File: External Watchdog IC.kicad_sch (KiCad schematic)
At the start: 10 parts, among them U10 TPS3823A-33DBVR, U9 TPS3823A-33DBVR

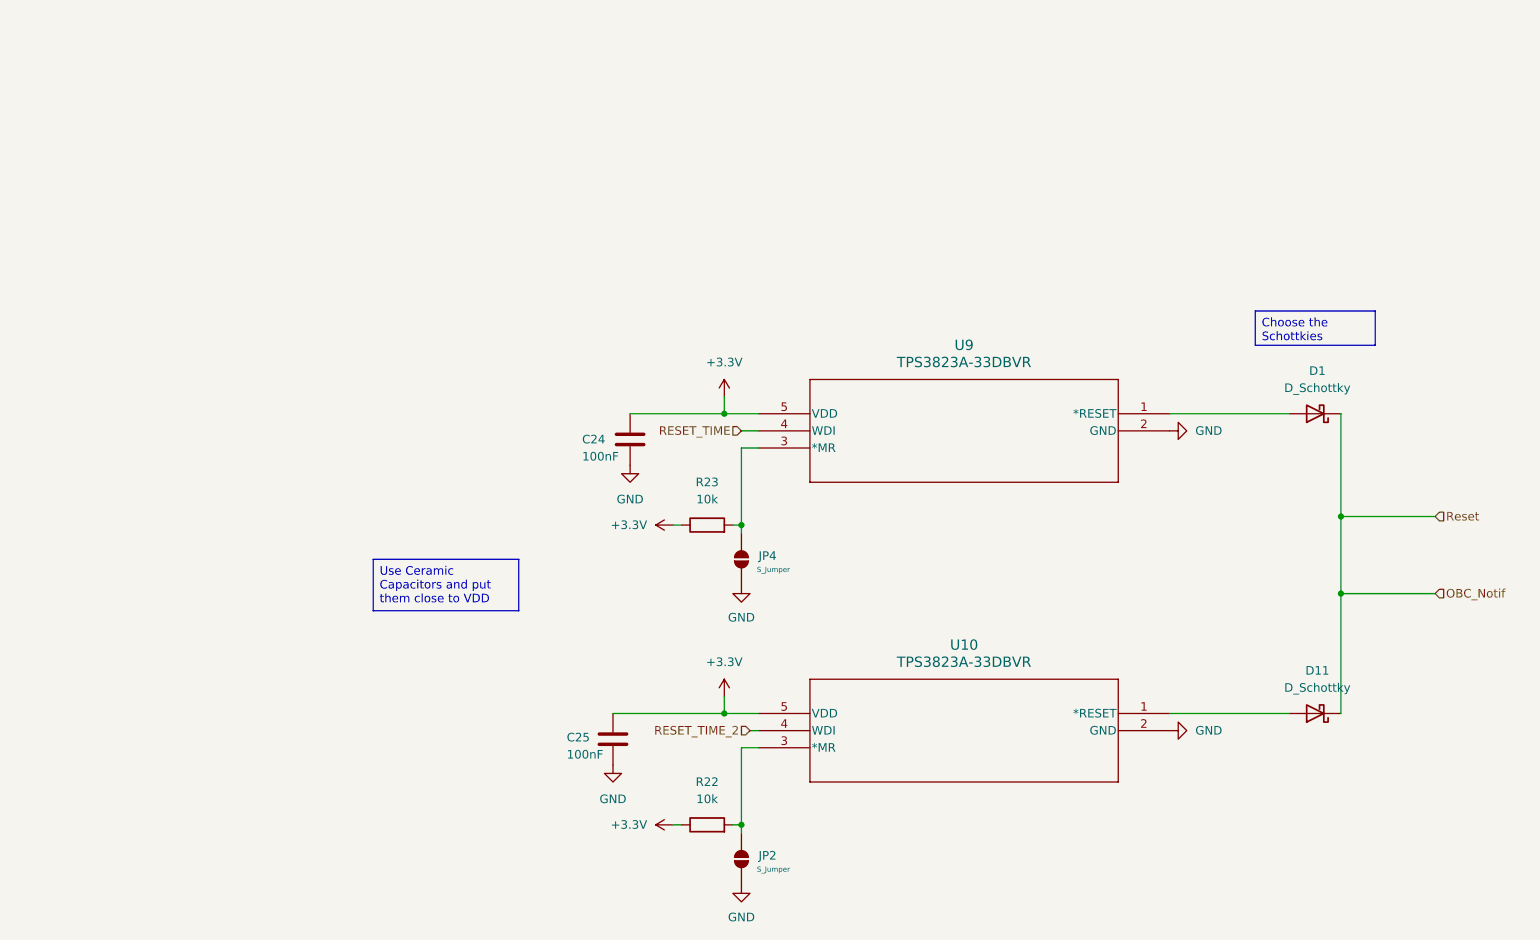
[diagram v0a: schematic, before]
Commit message: Added cap to output of lines
based on LTSpice Simulation
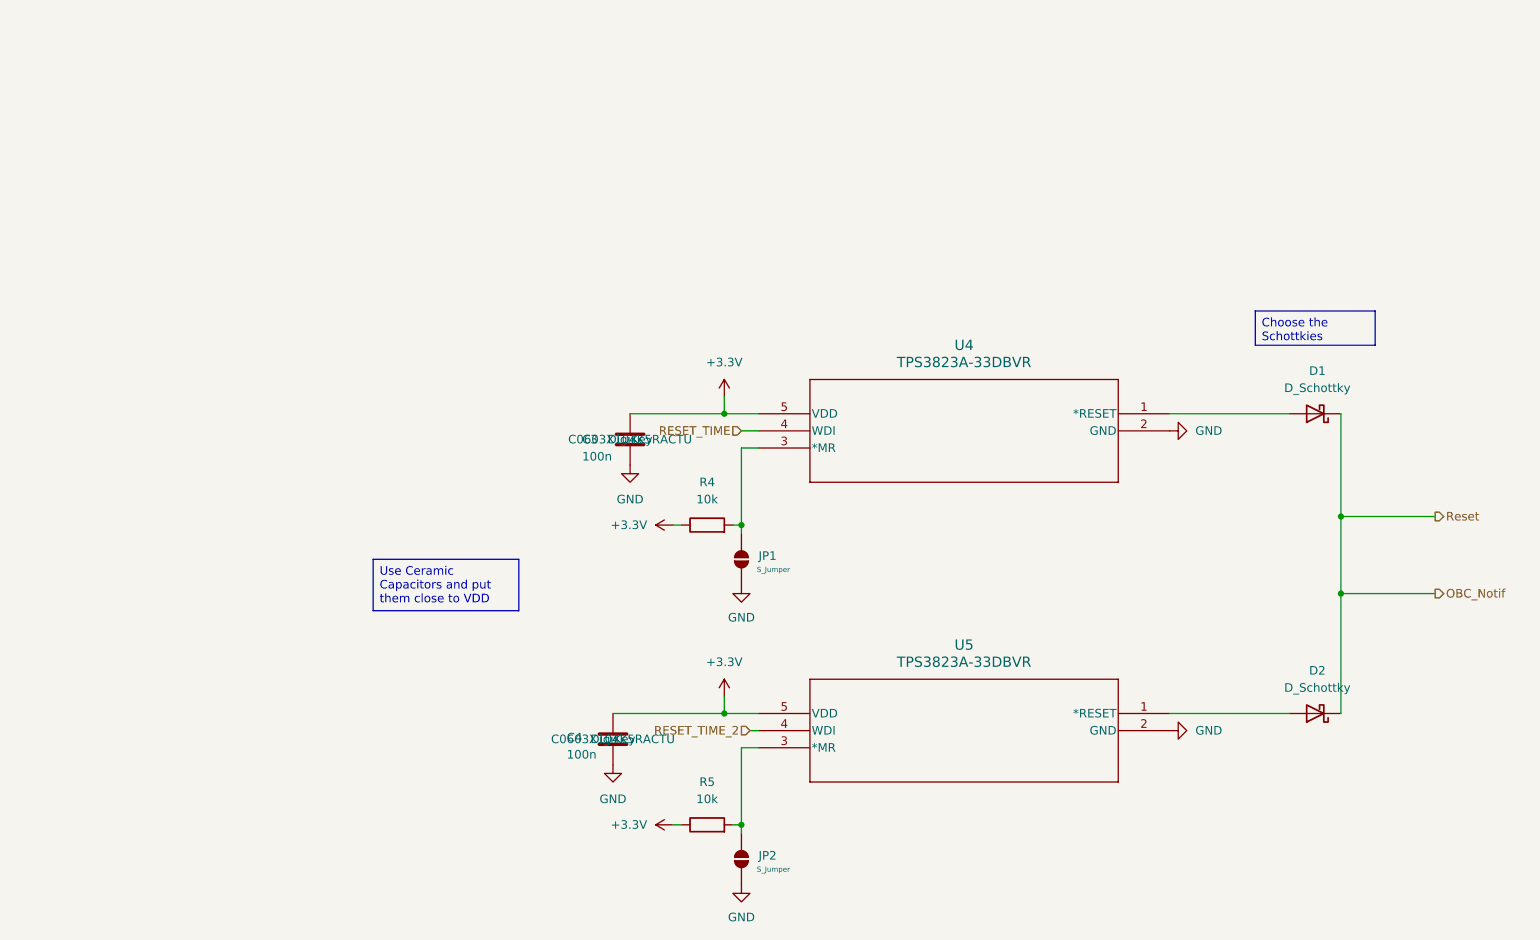
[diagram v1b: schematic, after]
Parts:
- C3: renamed from C24; value 100nF -> 100n; footprint (none) -> Capacitor_SMD:C_0603_1608Metric; MANUFACTURER (none) -> DigiKey; MANUFACTURER_PART_NUMBER (none) -> C0603X104K5RACTU
- C4: renamed from C25; value 100nF -> 100n; footprint (none) -> Capacitor_SMD:C_0603_1608Metric; MANUFACTURER (none) -> DigiKey; MANUFACTURER_PART_NUMBER (none) -> C0603X104K5RACTU
- U5: renamed from U10; footprint DBV5 -> DQC0010A
- renumbered D11 to D2, JP4 to JP1, R23 to R4, R22 to R5, U9 to U4
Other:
- company: (none) -> QSET (Jaron Cyna)
- title: (none) -> External Watchdog
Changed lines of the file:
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@@
 	(generator_version "9.0")
 	(paper "A4")
+	(title_block
+		(title "External Watchdog")
+		(date "2026-03-17")
+		(rev "1.0")
+		(company "QSET (Jaron Cyna)")
+	)
 	(text_box "Use Ceramic Capacitors and put them close to VDD"
 		(exclude_from_sim no)
@@
 	)
 	(hierarchical_label "Reset"
-		(shape input)
+		(shape output)
 		(at 220.98 87.63 0)
 		(effects
@@
 	)
 	(hierarchical_label "OBC_Notif"
-		(shape input)
+		(shape output)
 		(at 220.98 99.06 0)
 		(effects
@@
 		(dnp no)
 		(fields_autoplaced yes)
-		(property "Reference" "#PWR074"
+		(property "Reference" "#PWR016"
 			(at 111.76 133.35 0)
 			(effects
@@
 			(project "EPS_mppt_board"
 				(path "/8f246f89-1ec7-4136-9977-839b50e116ed/61eb8b07-a516-4600-8bd8-c85438ae98cc"
-					(reference "#PWR074")
+					(reference "#PWR016")
 					(unit 1)
 				)
@@
 		(dnp no)
 		(fields_autoplaced yes)
-		(property "Reference" "D11"
+		(property "Reference" "D2"
 			(at 203.5175 110.49 0)
 			(effects
@@
 			(project "EPS_mppt_board"
 				(path "/8f246f89-1ec7-4136-9977-839b50e116ed/61eb8b07-a516-4600-8bd8-c85438ae98cc"
-					(reference "D11")
+					(reference "D2")
 					(unit 1)
 				)
@@
 		(dnp no)
 		(fields_autoplaced yes)
-		(property "Reference" "#PWR071"
+		(property "Reference" "#PWR014"
 			(at 187.96 119.38 0)
 			(effects
@@
 			(project "EPS_mppt_board"
 				(path "/8f246f89-1ec7-4136-9977-839b50e116ed/61eb8b07-a516-4600-8bd8-c85438ae98cc"
-					(reference "#PWR071")
+					(reference "#PWR014")
 					(unit 1)
 				)
@@
 		(dnp no)
 		(fields_autoplaced yes)
-		(property "Reference" "#PWR067"
+		(property "Reference" "#PWR010"
 			(at 101.6 86.36 0)
 			(effects
@@
 			(project ""
 				(path "/8f246f89-1ec7-4136-9977-839b50e116ed/61eb8b07-a516-4600-8bd8-c85438ae98cc"
-					(reference "#PWR067")
+					(reference "#PWR010")
 					(unit 1)
 				)
@@
 		(on_board yes)
 		(dnp no)
-		(property "Reference" "U10"
+		(property "Reference" "U5"
 			(at 151.13 106.68 0)
 			(effects
@@
 			)
 		)
-		(property "Footprint" "DBV5"
+		(property "Footprint" "DQC0010A"
 			(at 181.61 116.84 0)
 			(effects
@@
 			(project "EPS_mppt_board"
 				(path "/8f246f89-1ec7-4136-9977-839b50e116ed/61eb8b07-a516-4600-8bd8-c85438ae98cc"
-					(reference "U10")
+					(reference "U5")
 					(unit 1)
 				)
@@
 		(dnp no)
 		(fields_autoplaced yes)
-		(property "Reference" "R23"
+		(property "Reference" "R4"
 			(at 113.03 82.55 90)
 			(effects
@@
 			(project "EPS_mppt_board"
 				(path "/8f246f89-1ec7-4136-9977-839b50e116ed/61eb8b07-a516-4600-8bd8-c85438ae98cc"
-					(reference "R23")
+					(reference "R4")
 					(unit 1)
 				)
@@
 		(on_board yes)
 		(dnp no)
-		(property "Reference" "C24"
+		(property "Reference" "C3"
 			(at 94.488 76.2 0)
 			(effects
@@
 			)
 		)
-		(property "Value" "100nF"
+		(property "Value" "100n"
 			(at 94.488 78.74 0)
 			(effects
@@
 			)
 		)
-		(property "Footprint" ""
+		(property "Footprint" "Capacitor_SMD:C_0603_1608Metric"
 			(at 102.5652 80.01 0)
 			(effects
@@
 			)
 		)
-		(property "Datasheet" "~"
+		(property "Datasheet" "kicad-embed://KEM_C1013_X7R_FT-CAP_SMD.pdf"
 			(at 101.6 76.2 0)
 			(effects
@@
 			)
 		)
-		(property "Description" "Unpolarized capacitor"
+		(property "Description" "kicad-embed://KEM_C1013_X7R_FT-CAP_SMD.pdf"
 			(at 101.6 76.2 0)
 			(effects
@@
 			)
 		)
+		(property "MANUFACTURER" "DigiKey"
+			(at 101.6 76.2 0)
+			(effects
+				(font
+					(size 1.27 1.27)
+				)
+			)
+		)
+		(property "MANUFACTURER_PART_NUMBER" "C0603X104K5RACTU"
+			(at 101.6 76.2 0)
+			(effects
+				(font
+					(size 1.27 1.27)
+				)
+			)
+		)
 		(pin "1"
 		)
@@
 			(project ""
 				(path "/8f246f89-1ec7-4136-9977-839b50e116ed/61eb8b07-a516-4600-8bd8-c85438ae98cc"
-					(reference "C24")
+					(reference "C3")
 					(unit 1)
 				)
@@
 		(dnp no)
 		(fields_autoplaced yes)
-		(property "Reference" "#PWR066"
+		(property "Reference" "#PWR08"
 			(at 115.57 73.66 0)
 			(effects
@@
 			(project ""
 				(path "/8f246f89-1ec7-4136-9977-839b50e116ed/61eb8b07-a516-4600-8bd8-c85438ae98cc"
-					(reference "#PWR066")
+					(reference "#PWR08")
 					(unit 1)
 				)
@@
 		(dnp no)
 		(fields_autoplaced yes)
-		(property "Reference" "R22"
+		(property "Reference" "R5"
 			(at 113.03 127 90)
 			(effects
@@
 			(project ""
 				(path "/8f246f89-1ec7-4136-9977-839b50e116ed/61eb8b07-a516-4600-8bd8-c85438ae98cc"
-					(reference "R22")
+					(reference "R5")
 					(unit 1)
 				)
@@
 		(on_board yes)
 		(dnp no)
-		(property "Reference" "C25"
+		(property "Reference" "C4"
 			(at 92.202 120.396 0)
 			(effects
@@
 			)
 		)
-		(property "Value" "100nF"
+		(property "Value" "100n"
 			(at 92.202 122.936 0)
 			(effects
@@
 			)
 		)
-		(property "Footprint" ""
+		(property "Footprint" "Capacitor_SMD:C_0603_1608Metric"
 			(at 100.0252 124.46 0)
 			(effects
@@
 			)
 		)
-		(property "Datasheet" "~"
+		(property "Datasheet" "kicad-embed://KEM_C1013_X7R_FT-CAP_SMD.pdf"
 			(at 99.06 120.65 0)
 			(effects
@@
 			)
 		)
-		(property "Description" "Unpolarized capacitor"
+		(property "Description" "kicad-embed://KEM_C1013_X7R_FT-CAP_SMD.pdf"
 			(at 99.06 120.65 0)
 			(effects
@@
 			)
 		)
+		(property "MANUFACTURER" "DigiKey"
+			(at 99.06 120.65 0)
+			(effects
+				(font
+					(size 1.27 1.27)
+				)
+			)
+		)
+		(property "MANUFACTURER_PART_NUMBER" "C0603X104K5RACTU"
+			(at 99.06 120.65 0)
+			(effects
+				(font
+					(size 1.27 1.27)
+				)
+			)
+		)
 		(pin "1"
 		)
@@
 			(project "EPS_mppt_board"
 				(path "/8f246f89-1ec7-4136-9977-839b50e116ed/61eb8b07-a516-4600-8bd8-c85438ae98cc"
-					(reference "C25")
+					(reference "C4")
 					(unit 1)
 				)
@@
 		(dnp no)
 		(fields_autoplaced yes)
-		(property "Reference" "#PWR075"
+		(property "Reference" "#PWR011"
 			(at 111.76 88.9 0)
 			(effects
@@
 			(project "EPS_mppt_board"
 				(path "/8f246f89-1ec7-4136-9977-839b50e116ed/61eb8b07-a516-4600-8bd8-c85438ae98cc"
-					(reference "#PWR075")
+					(reference "#PWR011")
 					(unit 1)
 				)
@@
 		(dnp no)
 		(fields_autoplaced yes)
-		(property "Reference" "#PWR069"
+		(property "Reference" "#PWR013"
 			(at 115.57 118.11 0)
 			(effects
@@
 			(project "EPS_mppt_board"
 				(path "/8f246f89-1ec7-4136-9977-839b50e116ed/61eb8b07-a516-4600-8bd8-c85438ae98cc"
-					(reference "#PWR069")
+					(reference "#PWR013")
 					(unit 1)
 				)
@@
 		(dnp no)
 		(fields_autoplaced yes)
-		(property "Reference" "#PWR068"
+		(property "Reference" "#PWR015"
 			(at 99.06 130.81 0)
 			(effects
@@
 			(project "EPS_mppt_board"
 				(path "/8f246f89-1ec7-4136-9977-839b50e116ed/61eb8b07-a516-4600-8bd8-c85438ae98cc"
-					(reference "#PWR068")
+					(reference "#PWR015")
 					(unit 1)
 				)
@@
 		(on_board yes)
 		(dnp no)
-		(property "Reference" "#PWR073"
+		(property "Reference" "#PWR017"
 			(at 118.11 148.59 0)
 			(effects
@@
 			(project "EPS_mppt_board"
 				(path "/8f246f89-1ec7-4136-9977-839b50e116ed/61eb8b07-a516-4600-8bd8-c85438ae98cc"
-					(reference "#PWR073")
+					(reference "#PWR017")
 					(unit 1)
 				)
@@
 		(on_board yes)
 		(dnp no)
-		(property "Reference" "U9"
+		(property "Reference" "U4"
 			(at 151.13 62.23 0)
 			(effects
@@
 			(project ""
 				(path "/8f246f89-1ec7-4136-9977-839b50e116ed/61eb8b07-a516-4600-8bd8-c85438ae98cc"
-					(reference "U9")
+					(reference "U4")
 					(unit 1)
 				)
@@
 		(on_board yes)
 		(dnp no)
-		(property "Reference" "JP4"
+		(property "Reference" "JP1"
 			(at 120.65 93.472 90)
 			(effects
@@
 			(project "EPS_mppt_board"
 				(path "/8f246f89-1ec7-4136-9977-839b50e116ed/61eb8b07-a516-4600-8bd8-c85438ae98cc"
-					(reference "JP4")
+					(reference "JP1")
 					(unit 1)
 				)
@@
 		(dnp no)
 		(fields_autoplaced yes)
-		(property "Reference" "#PWR070"
+		(property "Reference" "#PWR09"
 			(at 187.96 74.93 0)
 			(effects
@@
 			(project "EPS_mppt_board"
 				(path "/8f246f89-1ec7-4136-9977-839b50e116ed/61eb8b07-a516-4600-8bd8-c85438ae98cc"
-					(reference "#PWR070")
+					(reference "#PWR09")
 					(unit 1)
 				)
@@
 		(on_board yes)
 		(dnp no)
-		(property "Reference" "#PWR076"
+		(property "Reference" "#PWR012"
 			(at 118.11 104.14 0)
 			(effects
@@
 			(project "EPS_mppt_board"
 				(path "/8f246f89-1ec7-4136-9977-839b50e116ed/61eb8b07-a516-4600-8bd8-c85438ae98cc"
-					(reference "#PWR076")
-					(unit 1)
-				)
+					(reference "#PWR012")
+					(unit 1)
+				)

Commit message: Added footprints to caps
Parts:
- renumbered C3 to C4, C4 to C5
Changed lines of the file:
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@@
 		(on_board yes)
 		(dnp no)
-		(property "Reference" "C3"
+		(property "Reference" "C4"
 			(at 94.488 76.2 0)
 			(effects
@@
 			(project ""
 				(path "/8f246f89-1ec7-4136-9977-839b50e116ed/61eb8b07-a516-4600-8bd8-c85438ae98cc"
-					(reference "C3")
+					(reference "C4")
 					(unit 1)
 				)
@@
 		(on_board yes)
 		(dnp no)
-		(property "Reference" "C4"
+		(property "Reference" "C5"
 			(at 92.202 120.396 0)
 			(effects
@@
 			(project "EPS_mppt_board"
 				(path "/8f246f89-1ec7-4136-9977-839b50e116ed/61eb8b07-a516-4600-8bd8-c85438ae98cc"
-					(reference "C4")
-					(unit 1)
-				)
+					(reference "C5")
+					(unit 1)
+				)

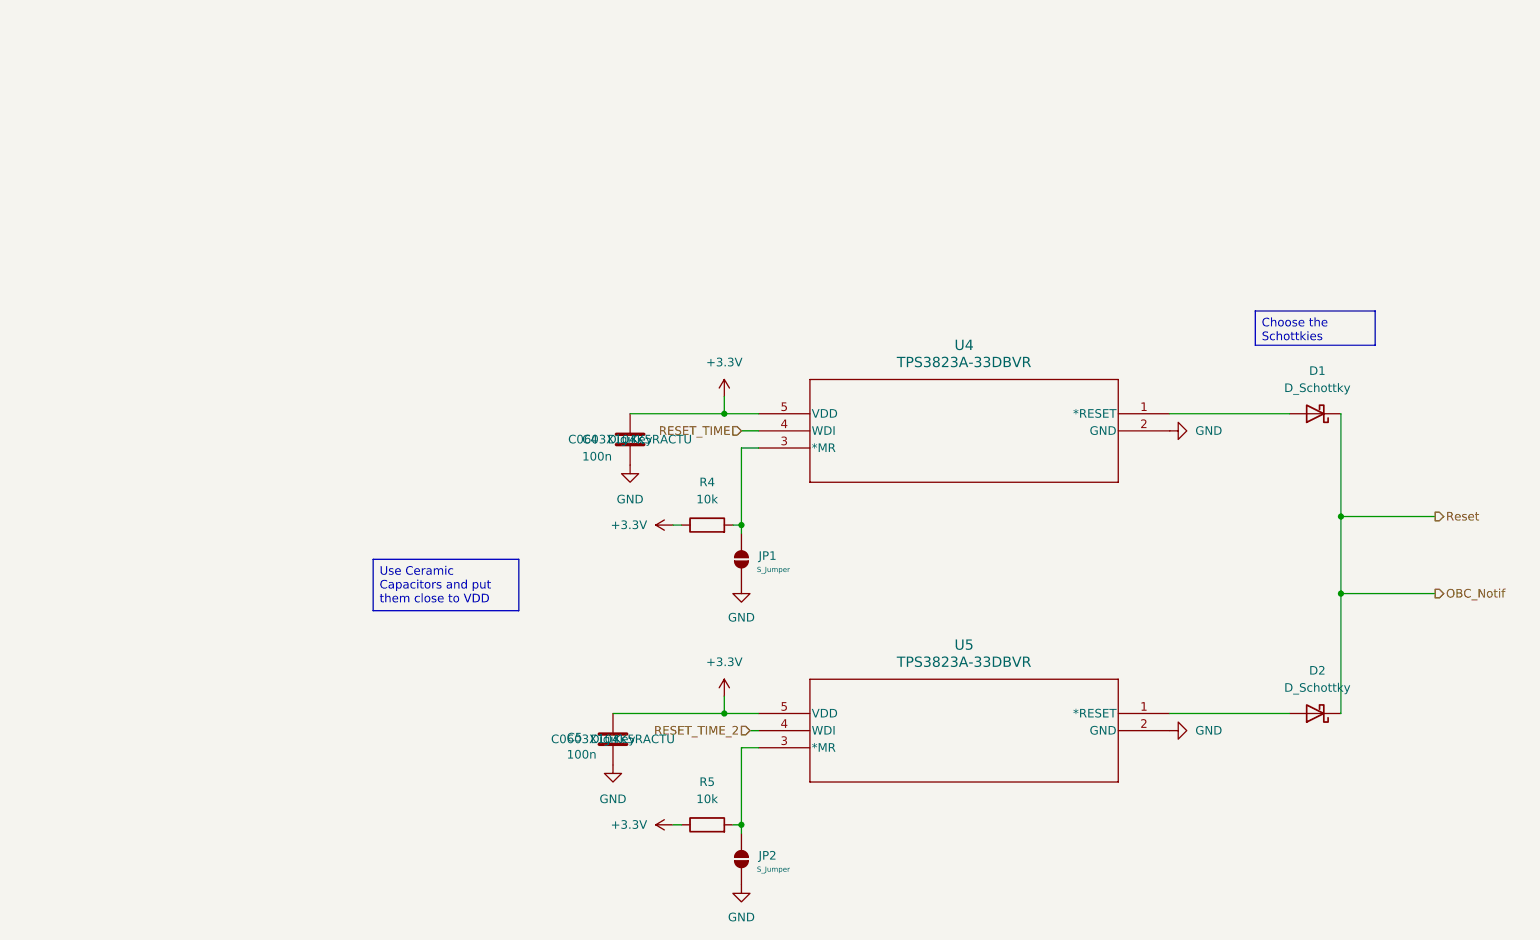
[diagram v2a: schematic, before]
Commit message: edited 3V3 Logic to add Efuse and UVLO
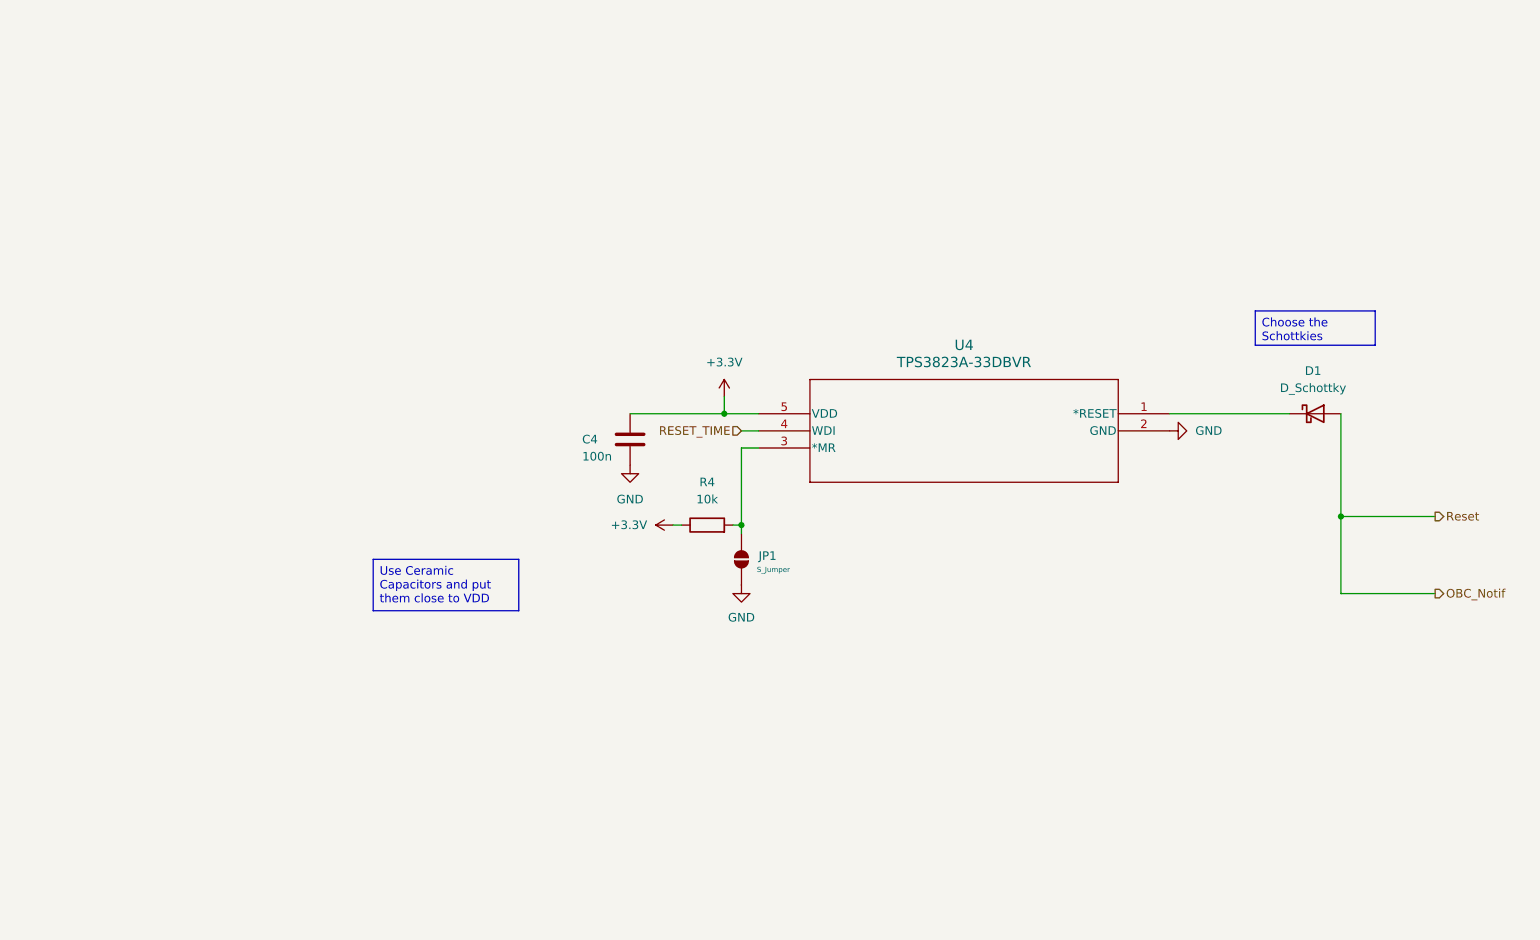
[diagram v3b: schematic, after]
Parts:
- removed C5: 100n, Capacitor_SMD:C_0603_1608Metric, symbol Device:C
- removed D2: D_Schottky, symbol Device:D_Schottky
- removed JP2: S_Jumper, Jumper:SolderJumper-2_P1.3mm_Open_TrianglePad1.0x1.5mm, symbol Jumper:SolderJumper_2_Open
- removed R5: 10k, symbol Device:R
- removed U5: TPS3823A-33DBVR, DQC0010A, symbol TPS3823:TPS3823-25DBVR
- D1: footprint (none) -> Diode_SMD:D_SOD-323F; MANUFACTURER (none) -> Digikey; MANUFACTURER_PART_NUMBER (none) -> RBE01VYM6AFHTR
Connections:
- net OBC_Notif: now also D1.2 (A); no longer D1.1 (K)
- net at U4.1 (*RESET): now also D1.1 (K); no longer D1.2 (A)
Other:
- moved on the sheet: D1
